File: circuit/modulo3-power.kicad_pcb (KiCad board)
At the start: 2 copper layers, 0 parts

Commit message: fv-1 mostly done; power progressed
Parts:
- added BT1: 25V, myAmp:XT60-M, F.Cu at (107.3, 97.2)
- added C1: 100nF, myAmp:C_1206, F.Cu at (62.9, 67.3)
- added C10: 47μF, myAmp:CPOL_D4_P1.5, F.Cu at (96.5, 59.1)
- added C2: 330n, myAmp:C_5.0MM, F.Cu at (120.7, 85.7)
- added C3: 100nF, myAmp:C_1206, F.Cu at (61.6, 80.0)
- added C4: 20μF, myAmp:CPOL_D6.3_P2.5, F.Cu at (57.1, 80.0)
- added C5: 20μF, myAmp:CPOL_D6.3_P2.5, F.Cu at (66.0, 80.0)
- added C6: 10μF, myAmp:C_1812, F.Cu at (68.6, 64.1)
- added C7: 10μF, myAmp:C_1812, F.Cu at (72.4, 64.1)
- added C8: 100nF, myAmp:C_1206, F.Cu at (96.5, 62.9)
- added C9: 10μF, myAmp:CPOL_D4_P1.5, F.Cu at (101.6, 65.4)
- added D1: 1N4148, myAmp:DO35, F.Cu at (65.4, 64.1)
- added D2: SS18A, myAmp:D_SMA, F.Cu at (57.8, 72.4)
- added D3: power, myAmp:LED_D3.0mm, F.Cu at (92.1, 97.8)
- added F1: 2A, myAmp:MF-LSMF, F.Cu at (106.7, 87.0)
- added J1: HOLE, myAmp:MountingHole, F.Cu at (54.0, 54.0)
- added J2: HOLE, myAmp:MountingHole, F.Cu at (130.0, 54.0)
- added J3: HOLE, myAmp:MountingHole, F.Cu at (54.0, 98.0)
- added J4: HOLE, myAmp:MountingHole, F.Cu at (130.0, 98.0)
- added L1: 27μH, myAmp:COIL_DER0705, F.Cu at (69.2, 72.4)
- added Q1: IRF4905SPBF, myAmp:D2PAK, F.Cu at (120.7, 73.7)
- added R1: 470k, myAmp:R_10MM, F.Cu at (120.7, 88.9)
- added R2: 75K, myAmp:R_0805, F.Cu at (61.0, 62.2)
- added R3: 10K, myAmp:R_0805, F.Cu at (58.4, 62.2)
- added R4: 1M, myAmp:R_10MM, F.Cu at (120.7, 91.4)
- added R5: 4k7, myAmp:R_10MM, F.Cu at (82.5, 97.8)
- added SW1: on/off, myAmp:SW_DPDT, F.Cu at (120.7, 98.0)
- added U1: MCP16331, myAmp:SOT-23-6, F.Cu at (59.7, 67.3)
- added U2: LM1117-5.0, myAmp:TO-252-3, F.Cu at (107.4, 59.7)
- added U3: PWR_CONN, myAmp:PWR_CONN, F.Cu at (121.0, 54.0)
- added U4: AMPCTRL, myAmp:AMPCTRL, F.Cu at (76.0, 54.0)
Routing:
- added copper zone on B.Cu, net GND
- added copper zone on F.Cu, net GND
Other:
- board outline added: 84 x 52 mm

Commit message: lotsa things :)
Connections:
- SW1 pad 5: unconnected-(SW1-Pad5) -> /MUTE
- SW1 pad 6: unconnected-(SW1-Pad6) -> GND
- U4 pad 3: unconnected-(U4-MUTE-Pad3) -> /MUTE
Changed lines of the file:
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@@
   (net 13 "unconnected-(U1-EN-Pad4)")
   (net 14 "unconnected-(U4-RESET-Pad2)")
-  (net 15 "unconnected-(U4-MUTE-Pad3)")
+  (net 15 "/MUTE")
   (net 16 "unconnected-(U4-FAULT-Pad4)")
   (net 17 "unconnected-(U4-OTW_CLIP-Pad5)")
   (net 18 "unconnected-(SW1-Pad3)")
   (net 19 "unconnected-(SW1-Pad4)")
-  (net 20 "unconnected-(SW1-Pad5)")
-  (net 21 "unconnected-(SW1-Pad6)")
   (footprint "myAmp:C_1812" (layer "F.Cu")
     (at 68.58 64.135 90)
@@
         (effects (font (size 0.75 0.75) (thickness 0.15)))
     )
-    (pad "1" thru_hole circle (at -1.27 2.54) (size 1.6 1.6) (drill 0.8) (layers "*.Cu" "*.Mask")
+    (pad "1" thru_hole circle (at -1.27 2.54) (size 1.6 1.6) (drill 0.9) (layers "*.Cu" "*.Mask")
       (net 5 "Net-(Q1-S)") (pintype "passive"))
-    (pad "2" thru_hole circle (at -1.27 0) (size 1.6 1.6) (drill 0.8) (layers "*.Cu" "*.Mask")
+    (pad "2" thru_hole circle (at -1.27 0) (size 1.6 1.6) (drill 0.9) (layers "*.Cu" "*.Mask")
       (net 11 "Net-(F1-Pad2)") (pintype "passive"))
-    (pad "3" thru_hole circle (at -1.27 -2.54) (size 1.6 1.6) (drill 0.8) (layers "*.Cu" "*.Mask")
+    (pad "3" thru_hole circle (at -1.27 -2.54) (size 1.6 1.6) (drill 0.9) (layers "*.Cu" "*.Mask")
       (net 18 "unconnected-(SW1-Pad3)") (pintype "passive+no_connect"))
-    (pad "4" thru_hole circle (at 1.27 2.54) (size 1.6 1.6) (drill 0.8) (layers "*.Cu" "*.Mask")
+    (pad "4" thru_hole circle (at 1.27 2.54) (size 1.6 1.6) (drill 0.9) (layers "*.Cu" "*.Mask")
       (net 19 "unconnected-(SW1-Pad4)") (pintype "passive+no_connect"))
-    (pad "5" thru_hole circle (at 1.27 0) (size 1.6 1.6) (drill 0.8) (layers "*.Cu" "*.Mask")
-      (net 20 "unconnected-(SW1-Pad5)") (pintype "passive"))
-    (pad "6" thru_hole circle (at 1.27 -2.54) (size 1.6 1.6) (drill 0.8) (layers "*.Cu" "*.Mask")
-      (net 21 "unconnected-(SW1-Pad6)") (pintype "passive"))
+    (pad "5" thru_hole circle (at 1.27 0) (size 1.6 1.6) (drill 0.9) (layers "*.Cu" "*.Mask")
+      (net 15 "/MUTE") (pintype "passive"))
+    (pad "6" thru_hole circle (at 1.27 -2.54) (size 1.6 1.6) (drill 0.9) (layers "*.Cu" "*.Mask")
+      (net 1 "GND") (pintype "passive"))
     (model "${KIPRJMOD}/myAmp.pretty/models/PinHeader_2x03_P2.54mm_Horizontal.wrl"
       (offset (xyz -1.27 2.54 0))
@@
     )
   )
-  (footprint "myAmp:AMPCTRL" (layer "F.Cu")
-    (at 76 54)
-    (property "Sheetfile" "modulo3-power.kicad_sch")
-    (property "Sheetname" "")
-    (attr through_hole)
-    (fp_text reference "U4" (at -7.62 0 unlocked) (layer "F.SilkS") hide
-        (effects (font (size 0.75 0.75) (thickness 0.15)))
-    )
-    (fp_text value "AMPCTRL" (at 0 1 unlocked) (layer "F.Fab") hide
-        (effects (font (size 1 1) (thickness 0.15)))
-    )
-    (fp_text user "FLT" (at 0 -1.27 90 unlocked) (layer "F.SilkS")
-        (effects (font (size 0.75 0.75) (thickness 0.15)) (justify left))
-    )
-    (fp_text user "MUT" (at -2.54 -1.27 90 unlocked) (layer "F.SilkS")
-        (effects (font (size 0.75 0.75) (thickness 0.15)) (justify left))
-    )
-    (fp_text user "GND" (at 5.08 -1.27 90 unlocked) (layer "F.SilkS")
-        (effects (font (size 0.75 0.75) (thickness 0.15)) (justify left))
-    )
-    (fp_text user "O/C" (at 2.54 -1.27 90 unlocked) (layer "F.SilkS")
-        (effects (font (size 0.75 0.75) (thickness 0.15)) (justify left))
-    )
-    (fp_text user "RST" (at -5.08 -1.27 90 unlocked) (layer "F.SilkS")
-        (effects (font (size 0.75 0.75) (thickness 0.15)) (justify left))
-    )
-    (pad "1" thru_hole roundrect (at 5.08 0) (size 1.6 1.6) (drill 0.8) (layers "*.Cu" "*.Mask") (roundrect_rratio 0.25)
-      (net 1 "GND") (pinfunction "GND") (pintype "input"))
-    (pad "2" thru_hole circle (at -5.08 0) (size 1.6 1.6) (drill 0.8) (layers "*.Cu" "*.Mask")
-      (net 14 "unconnected-(U4-RESET-Pad2)") (pinfunction "RESET") (pintype "input"))
-    (pad "3" thru_hole circle (at -2.54 0) (size 1.6 1.6) (drill 0.8) (layers "*.Cu" "*.Mask")
-      (net 15 "unconnected-(U4-MUTE-Pad3)") (pinfunction "MUTE") (pintype "input"))
-    (pad "4" thru_hole circle (at 0 0) (size 1.6 1.6) (drill 0.8) (layers "*.Cu" "*.Mask")
-      (net 16 "unconnected-(U4-FAULT-Pad4)") (pinfunction "FAULT") (pintype "output+no_connect"))
-    (pad "5" thru_hole circle (at 2.54 0) (size 1.6 1.6) (drill 0.8) (layers "*.Cu" "*.Mask")
-      (net 17 "unconnected-(U4-OTW_CLIP-Pad5)") (pinfunction "OTW_CLIP") (pintype "output+no_connect"))
-    (model "${KIPRJMOD}/myAmp.pretty/models/PinHeader_1x05_P2.54mm_Vertical.wrl"
-      (offset (xyz 5.08 0 0))
-      (scale (xyz 1 1 1))
-      (rotate (xyz 0 0 90))
-    )
-  )
   (footprint "myAmp:MountingHole" (layer "F.Cu")
     (at 54 54)
@@
       (scale (xyz 1 1 1))
       (rotate (xyz 0 0 0))
+    )
+  )
+  (footprint "myAmp:AMPCTRL" (layer "F.Cu")
+    (at 76 54)
+    (property "Sheetfile" "modulo3-power.kicad_sch")
+    (property "Sheetname" "")
+    (attr through_hole)
+    (fp_text reference "U4" (at -7.62 0 unlocked) (layer "F.SilkS") hide
+        (effects (font (size 0.75 0.75) (thickness 0.15)))
+    )
+    (fp_text value "AMPCTRL" (at 0 1 unlocked) (layer "F.Fab") hide
+        (effects (font (size 1 1) (thickness 0.15)))
+    )
+    (fp_text user "O/C" (at 2.54 -1.27 90 unlocked) (layer "F.SilkS")
+        (effects (font (size 0.75 0.75) (thickness 0.15)) (justify left))
+    )
+    (fp_text user "RST" (at -5.08 -1.27 90 unlocked) (layer "F.SilkS")
+        (effects (font (size 0.75 0.75) (thickness 0.15)) (justify left))
+    )
+    (fp_text user "FLT" (at 0 -1.27 90 unlocked) (layer "F.SilkS")
+        (effects (font (size 0.75 0.75) (thickness 0.15)) (justify left))
+    )
+    (fp_text user "GND" (at 5.08 -1.27 90 unlocked) (layer "F.SilkS")
+        (effects (font (size 0.75 0.75) (thickness 0.15)) (justify left))
+    )
+    (fp_text user "MUT" (at -2.54 -1.27 90 unlocked) (layer "F.SilkS")
+        (effects (font (size 0.75 0.75) (thickness 0.15)) (justify left))
+    )
+    (pad "1" thru_hole roundrect (at 5.08 0) (size 1.6 1.6) (drill 0.9) (layers "*.Cu" "*.Mask") (roundrect_rratio 0.25)
+      (net 1 "GND") (pinfunction "GND") (pintype "input"))
+    (pad "2" thru_hole circle (at -5.08 0) (size 1.6 1.6) (drill 0.9) (layers "*.Cu" "*.Mask")
+      (net 14 "unconnected-(U4-RESET-Pad2)") (pinfunction "RESET") (pintype "input+no_connect"))
+    (pad "3" thru_hole circle (at -2.54 0) (size 1.6 1.6) (drill 0.9) (layers "*.Cu" "*.Mask")
+      (net 15 "/MUTE") (pinfunction "MUTE") (pintype "input"))
+    (pad "4" thru_hole circle (at 0 0) (size 1.6 1.6) (drill 0.9) (layers "*.Cu" "*.Mask")
+      (net 16 "unconnected-(U4-FAULT-Pad4)") (pinfunction "FAULT") (pintype "output+no_connect"))
+    (pad "5" thru_hole circle (at 2.54 0) (size 1.6 1.6) (drill 0.9) (layers "*.Cu" "*.Mask")
+      (net 17 "unconnected-(U4-OTW_CLIP-Pad5)") (pinfunction "OTW_CLIP") (pintype "output+no_connect"))
+    (model "${KIPRJMOD}/myAmp.pretty/models/PinHeader_1x05_P2.54mm_Vertical.wrl"
+      (offset (xyz 5.08 0 0))
+      (scale (xyz 1 1 1))
+      (rotate (xyz 0 0 90))
     )
   )
@@
         (effects (font (size 0.75 0.75) (thickness 0.15)) (justify left))
     )
-    (pad "1" thru_hole roundrect (at 2.54 0 180) (size 1.6 1.6) (drill 0.8) (layers "*.Cu" "*.Mask") (roundrect_rratio 0.25)
+    (pad "1" thru_hole roundrect (at 2.54 0 180) (size 1.6 1.6) (drill 0.9) (layers "*.Cu" "*.Mask") (roundrect_rratio 0.25)
       (net 1 "GND") (pinfunction "GND") (pintype "passive"))
-    (pad "2" thru_hole circle (at 0 0 180) (size 1.6 1.6) (drill 0.8) (layers "*.Cu" "*.Mask")
+    (pad "2" thru_hole circle (at 0 0 180) (size 1.6 1.6) (drill 0.9) (layers "*.Cu" "*.Mask")
       (net 7 "+BATT") (pinfunction "30V") (pintype "passive"))
-    (pad "3" thru_hole circle (at -2.54 0 180) (size 1.6 1.6) (drill 0.8) (layers "*.Cu" "*.Mask")
+    (pad "3" thru_hole circle (at -2.54 0 180) (size 1.6 1.6) (drill 0.9) (layers "*.Cu" "*.Mask")
       (net 9 "+5V") (pinfunction "5V") (pintype "passive"))
     (model "${KIPRJMOD}/myAmp.pretty/models/PinHeader_1x03_P2.54mm_Vertical.step"
@@
     (stroke (width 0.1) (type default)) (layer "Edge.Cuts"))
   (zone (net 1) (net_name "GND") (layers "F&B.Cu") (hatch edge 0.5)
-    (connect_pads (clearance 0.5))
-    (min_thickness 0.25) (filled_areas_thickness no)
-    (fill yes (thermal_gap 0.5) (thermal_bridge_width 0.5))
+    (connect_pads (clearance 0.254))
+    (min_thickness 0.254) (filled_areas_thickness no)
+    (fill yes (thermal_gap 0.254) (thermal_bridge_width 0.254))
     (polygon
       (pts

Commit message: futher...
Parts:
- BT1: moved to B.Cu
- moved BT1 0.90 mm to (106.7, 96.5)
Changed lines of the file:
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@@
     )
-  )
-  (footprint "myAmp:XT60-M" (layer "F.Cu")
-    (at 107.315 97.155 180)
-    (property "Sheetfile" "modulo3-power.kicad_sch")
-    (property "Sheetname" "")
-    (attr through_hole)
-    (fp_text reference "BT1" (at 0 3.175) (layer "F.SilkS")
-        (effects (font (size 0.75 0.75) (thickness 0.15)))
-    )
-    (fp_text value "25V" (at 10.16 0) (layer "F.SilkS")
-        (effects (font (size 1.2 1.2) (thickness 0.2)))
-    )
-    (fp_line (start -7.75 -2) (end -7.75 2)
-      (stroke (width 0.2) (type solid)) (layer "F.SilkS"))
-    (fp_line (start -7.75 2) (end -5 4.05)
-      (stroke (width 0.2) (type solid)) (layer "F.SilkS"))
-    (fp_line (start -5 -4.05) (end -7.75 -2)
-      (stroke (width 0.2) (type solid)) (layer "F.SilkS"))
-    (fp_line (start -5 -4.05) (end 7.75 -4.05)
-      (stroke (width 0.2) (type solid)) (layer "F.SilkS"))
-    (fp_line (start -5 4.05) (end 7.75 4.05)
-      (stroke (width 0.2) (type solid)) (layer "F.SilkS"))
-    (fp_line (start 7.75 -4.05) (end 7.75 4.05)
-      (stroke (width 0.2) (type solid)) (layer "F.SilkS"))
-    (pad "1" thru_hole circle (at 3.6 0 180) (size 6 6) (drill 4.5) (layers "*.Cu" "*.Mask")
-      (net 2 "Net-(BT1-+)") (pinfunction "+") (pintype "power_in"))
-    (pad "2" thru_hole circle (at -3.6 0 180) (size 6 6) (drill 4.5) (layers "*.Cu" "*.Mask")
-      (net 1 "GND") (pinfunction "-") (pintype "power_in"))
   )
   (footprint "myAmp:COIL_DER0705" (layer "F.Cu")
@@
     )
   )
+  (footprint "myAmp:XT60-M" (layer "B.Cu")
+    (at 106.68 96.52 180)
+    (property "Sheetfile" "modulo3-power.kicad_sch")
+    (property "Sheetname" "")
+    (attr through_hole)
+    (fp_text reference "BT1" (at 0 5) (layer "B.SilkS")
+        (effects (font (size 0.75 0.75) (thickness 0.15)) (justify mirror))
+    )
+    (fp_text value "25V" (at 0 -5.5) (layer "B.SilkS")
+        (effects (font (size 1.2 1.2) (thickness 0.2)) (justify mirror))
+    )
+    (fp_line (start -7.75 -2) (end -5 -4.05)
+      (stroke (width 0.2) (type solid)) (layer "B.SilkS"))
+    (fp_line (start -7.75 2) (end -7.75 -2)
+      (stroke (width 0.2) (type solid)) (layer "B.SilkS"))
+    (fp_line (start -5 -4.05) (end 7.75 -4.05)
+      (stroke (width 0.2) (type solid)) (layer "B.SilkS"))
+    (fp_line (start -5 4.05) (end -7.75 2)
+      (stroke (width 0.2) (type solid)) (layer "B.SilkS"))
+    (fp_line (start -5 4.05) (end 7.75 4.05)
+      (stroke (width 0.2) (type solid)) (layer "B.SilkS"))
+    (fp_line (start 7.75 4.05) (end 7.75 -4.05)
+      (stroke (width 0.2) (type solid)) (layer "B.SilkS"))
+    (pad "1" thru_hole circle (at 3.6 0 180) (size 6 6) (drill 4.5) (layers "*.Cu" "*.Mask")
+      (net 2 "Net-(BT1-+)") (pinfunction "+") (pintype "power_in"))
+    (pad "2" thru_hole circle (at -3.6 0 180) (size 6 6) (drill 4.5) (layers "*.Cu" "*.Mask")
+      (net 1 "GND") (pinfunction "-") (pintype "power_in"))
+    (model "${KIPRJMOD}/myAmp.pretty/models/XT60FemaleConnector.STEP"
+      (offset (xyz 1.46 0 8.1))
+      (scale (xyz 1 1 1))
+      (rotate (xyz 0 -90 0))
+    )
+  )

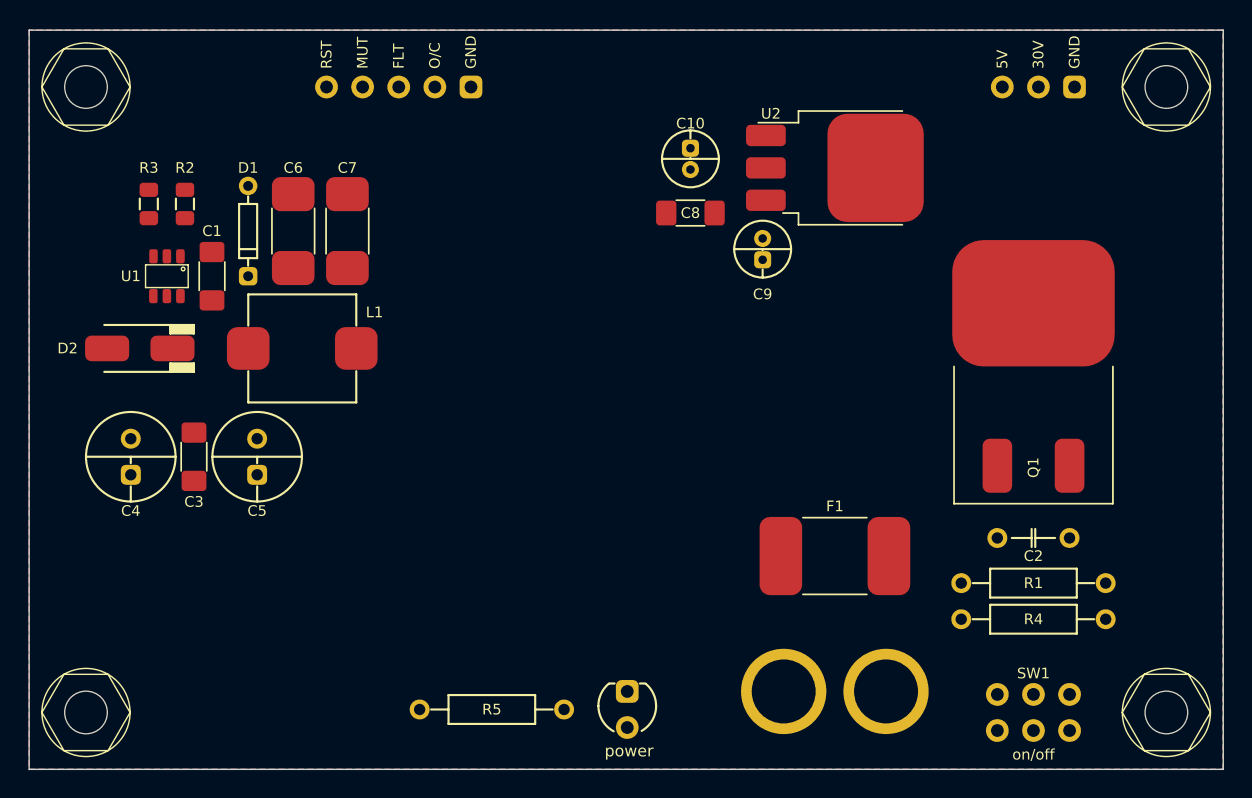
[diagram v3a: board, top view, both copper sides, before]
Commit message: tweaked power amp and fv1
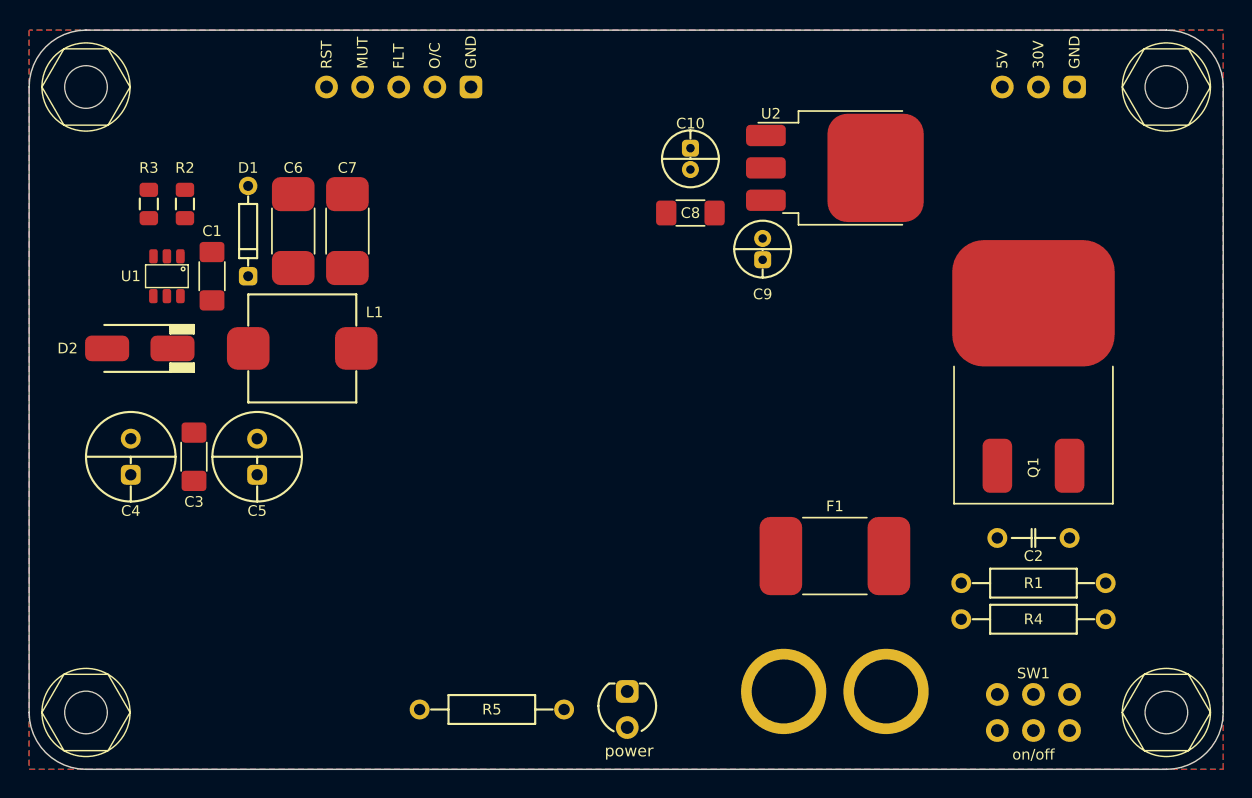
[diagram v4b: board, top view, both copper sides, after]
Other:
- outline, holes or cut-outs redrawn
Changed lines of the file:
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@@
         (effects (font (size 0.75 0.75) (thickness 0.15)) (justify mirror))
     )
-    (fp_text value "25V" (at 0 -5.5) (layer "B.SilkS")
+    (fp_text value "25V" (at 6.35 5.08) (layer "B.SilkS")
         (effects (font (size 1.2 1.2) (thickness 0.2)) (justify mirror))
     )
@@
     )
   )
-  (gr_line (start 134 50) (end 50 50)
+  (gr_line (start 130 50) (end 54 50)
     (stroke (width 0.1) (type default)) (layer "Edge.Cuts"))
-  (gr_line (start 134 102) (end 134 50)
+  (gr_line (start 134 98) (end 134 54)
     (stroke (width 0.1) (type default)) (layer "Edge.Cuts"))
-  (gr_line (start 50 102) (end 134 102)
+  (gr_line (start 54 102) (end 130 102)
     (stroke (width 0.1) (type default)) (layer "Edge.Cuts"))
-  (gr_line (start 50 50) (end 50 102)
+  (gr_arc (start 130 50) (mid 132.828427 51.171573) (end 134 54)
+    (stroke (width 0.1) (type default)) (layer "Edge.Cuts"))
+  (gr_arc (start 54 102) (mid 51.171573 100.828427) (end 50 98)
+    (stroke (width 0.1) (type default)) (layer "Edge.Cuts"))
+  (gr_arc (start 134 98) (mid 132.828427 100.828427) (end 130 102)
+    (stroke (width 0.1) (type default)) (layer "Edge.Cuts"))
+  (gr_line (start 50 54) (end 50 98)
+    (stroke (width 0.1) (type default)) (layer "Edge.Cuts"))
+  (gr_arc (start 50 54) (mid 51.171573 51.171573) (end 54 50)
     (stroke (width 0.1) (type default)) (layer "Edge.Cuts"))
   (zone (net 1) (net_name "GND") (layers "F&B.Cu") (hatch edge 0.5)
     (connect_pads (clearance 0.254))
     (min_thickness 0.254) (filled_areas_thickness no)
-    (fill yes (thermal_gap 0.254) (thermal_bridge_width 0.254))
+    (fill (thermal_gap 0.254) (thermal_bridge_width 0.254))
     (polygon
       (pts

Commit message: ready to panelize
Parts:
- moved SW1 74.2 mm to (55.2, 62.9), turned to 0 degrees
- moved R4 63.3 mm to (63.5, 64.1), turned to -90 degrees
- moved D2 61.1 mm to (117.5, 85.5), turned to -90 degrees
- moved R1 60.0 mm to (66.0, 64.1), turned to -90 degrees
- moved R3 57.7 mm to (114.9, 74.1)
- moved C6 57.6 mm to (125.1, 75.4)
- moved C7 57.6 mm to (128.9, 75.4)
- moved L1 57.6 mm to (125.7, 83.6)
- moved U1 57.6 mm to (116.2, 78.5)
- moved C1 57.6 mm to (119.4, 78.5)
- moved R2 57.1 mm to (116.8, 74.1)
- moved D1 57.0 mm to (121.3, 75.4)
- moved C2 55.8 mm to (69.2, 64.1), turned to 90 degrees
- moved C4 52.7 mm to (109.9, 77.9), turned to 180 degrees
- moved F1 52.4 mm to (55.9, 74.3), turned to 90 degrees
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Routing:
- net GND: track 0.00 -> 99.8 mm, vias 0 -> 33
- net 6V8: track 0.00 -> 40.5 mm
- net +BATT: track 0.00 -> 26.4 mm
- net Net-(Q1-S): track 0.00 -> 25.8 mm
- net /MUTE: track 0.00 -> 22.5 mm
- net +5V: track 0.00 -> 20.5 mm
- net Net-(Q1-G): track 0.00 -> 13.8 mm
- net Net-(F1-Pad2): track 0.00 -> 11.6 mm
- net Net-(D2-K): track 0.00 -> 10.7 mm
- net Net-(BT1-+): track 0.00 -> 8.27 mm
- net Net-(D1-K): track 0.00 -> 4.96 mm
- net Net-(U1-VFB): track 0.00 -> 4.08 mm
- net Net-(D3-A): track 0.00 -> 3.81 mm
- added copper zone on F.Cu, net +BATT
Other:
- board text added: "2023/03/19"
- board text added: "modulo3-power"

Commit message: attempt to send to fab: part II
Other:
- board text added: "2023/04/16"
- board text removed: "2023/03/19"
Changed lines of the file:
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@@
   (gr_arc (start 50 54) (mid 51.171573 51.171573) (end 54 50)
     (stroke (width 0.1) (type default)) (layer "Edge.Cuts"))
-  (gr_text "2023/03/19" (at 67.58 99.25) (layer "F.SilkS")
+  (gr_text "2023/04/16" (at 67.58 99.25) (layer "F.SilkS")
     (effects (font (size 2 2) (thickness 0.3)))
   )
